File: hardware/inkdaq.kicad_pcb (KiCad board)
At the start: 2 copper layers, 13.5 x 42.5 mm, 3 parts, among them U1 INA333xxDRG

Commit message: route pcb
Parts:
- removed R1: 2.05k, Resistor_SMD:R_0201_0603Metric
- removed U1: INA333xxDRG, Package_SON:WSON-8-1EP_3x3mm_P0.5mm_EP1.45x2.4mm
- added C1: 100nF, Capacitor_SMD:C_0201_0603Metric, F.Cu at (179.1, 126.7)
- added J1: Conn_01x01, inkdaq_footprints:WirePad_1mm_Square, F.Cu at (180.8, 133.0)
- added J2: Conn_01x01, inkdaq_footprints:WirePad_1mm_Square, F.Cu at (176.4, 132.8)
- added J3: Conn_01x01, inkdaq_footprints:WirePad_1mm_Square, F.Cu at (177.9, 133.2)
- added J4: Conn_01x01, inkdaq_footprints:WirePad_1mm_Square, F.Cu at (179.3, 133.3)
- moved B1 49.1 mm to (178.8, 131.1)
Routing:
- net HSFPAR_V_NEG: track 33.7 -> 6.00 mm, vias 2 -> 0
- net HSFPAR_V_POS: track 32.1 -> 4.60 mm
- net GND: track 8.10 -> 4.18 mm
- net VDD: track 9.80 -> 6.86 mm
- net Net-(R1-Pad1): track 2.24 -> 0.00 mm
- net Net-(R1-Pad2): track 2.16 -> 0.00 mm
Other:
- board size 13.5 x 42.5 mm -> 12 x 12 mm

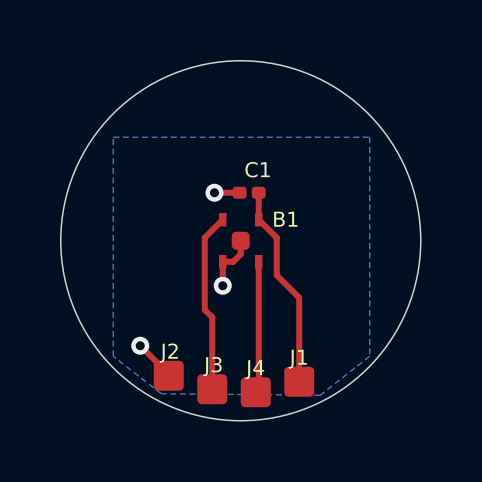
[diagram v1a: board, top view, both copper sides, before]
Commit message: make pcb 3mm radius and not 6mm (i thought it was the diameter lol)
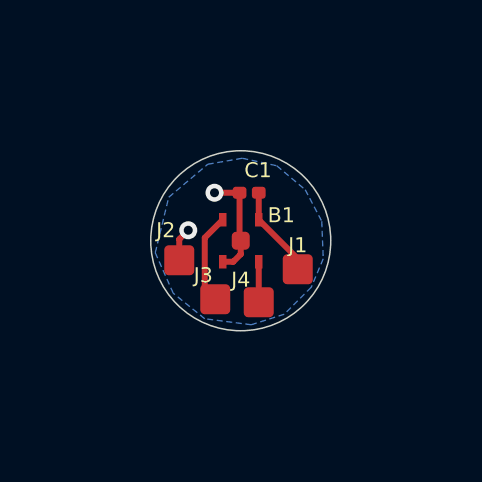
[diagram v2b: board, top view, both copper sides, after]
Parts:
- moved J2 3.87 mm to (176.8, 128.9)
- moved J1 3.75 mm to (180.8, 129.2)
- moved J3 3.00 mm to (178.0, 130.2)
- moved J4 3.00 mm to (179.4, 130.3)
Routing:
- net VDD: track 6.86 -> 3.09 mm
- net HSFPAR_V_POS: track 4.60 -> 1.35 mm
- net HSFPAR_V_NEG: track 6.00 -> 3.04 mm
- net GND: track 4.18 -> 4.73 mm, vias 3 -> 2
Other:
- board size 12 x 12 mm -> 6 x 6 mm
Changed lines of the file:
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@@
 	(footprint "inkdaq_footprints:WirePad_1mm_Square"
 		(layer "F.Cu")
-		(at 176.45 132.8)
+		(at 176.8 128.95)
 		(property "Reference" "J2"
-			(at 0.05 -0.8 0)
+			(at -0.45 -1 0)
 			(unlocked yes)
 			(layer "F.SilkS")
@@
 	(footprint "inkdaq_footprints:WirePad_1mm_Square"
 		(layer "F.Cu")
-		(at 180.8 133)
+		(at 180.75 129.25)
 		(property "Reference" "J1"
 			(at 0 -0.8 0)
@@
 	(footprint "inkdaq_footprints:WirePad_1mm_Square"
 		(layer "F.Cu")
-		(at 177.9 133.25)
+		(at 178 130.25)
 		(property "Reference" "J3"
-			(at 0.05 -0.8 0)
+			(at -0.4 -0.8 0)
 			(unlocked yes)
 			(layer "F.SilkS")
@@
 	(footprint "inkdaq_footprints:WirePad_1mm_Square"
 		(layer "F.Cu")
-		(at 179.35 133.35)
+		(at 179.45 130.35)
 		(property "Reference" "J4"
-			(at 0 -0.8 0)
+			(at -0.6 -0.75 0)
 			(unlocked yes)
 			(layer "F.SilkS")
@@
 		(descr "ALPSALPINE HSFPAR Series High-sensitivity Force Sensor")
 		(property "Reference" "B1"
-			(at 1.5 -3.45 0)
+			(at 1.35 -3.6 0)
 			(unlocked yes)
 			(layer "F.SilkS")
@@
 	(gr_circle
 		(center 178.85 128.3)
-		(end 184.85 128.3)
+		(end 181.85 128.3)
 		(stroke
 			(width 0.05)
@@
 	)
 	(segment
+		(start 178.81 128.26)
+		(end 178.85 128.3)
+		(width 0.2)
+		(layer "F.Cu")
+		(net 1)
+	)
+	(segment
 		(start 178.6 129)
 		(end 178.25 129)
@@
 	)
 	(segment
-		(start 176.45 132.8)
-		(end 176.45 132.75)
-		(width 0.2)
-		(layer "F.Cu")
-		(net 1)
-	)
-	(segment
-		(start 178.25 129.8)
-		(end 178.25 129)
-		(width 0.2)
-		(layer "F.Cu")
-		(net 1)
-	)
-	(segment
 		(start 178.85 128.75)
 		(end 178.6 129)
@@
 	)
 	(segment
+		(start 177.1 127.95)
+		(end 176.8 128.25)
+		(width 0.2)
+		(layer "F.Cu")
+		(net 1)
+	)
+	(segment
 		(start 177.975 126.7)
 		(end 178.81 126.7)
@@
 	)
 	(segment
-		(start 176.45 132.75)
-		(end 175.5 131.8)
+		(start 176.8 128.25)
+		(end 176.8 128.95)
+		(width 0.2)
+		(layer "F.Cu")
+		(net 1)
+	)
+	(segment
+		(start 178.81 126.7)
+		(end 178.81 128.26)
 		(width 0.2)
 		(layer "F.Cu")
@@
 	)
 	(via
-		(at 175.5 131.8)
+		(at 177.1 127.95)
 		(size 0.6)
 		(drill 0.3)
@@
 		(net 1)
 	)
-	(via
-		(at 178.25 129.8)
-		(size 0.6)
-		(drill 0.3)
-		(layers "F.Cu" "B.Cu")
-		(free yes)
-		(net 1)
-	)
-	(segment
-		(start 179.45 133.4)
-		(end 179.3 133.55)
+	(segment
+		(start 179.45 129)
+		(end 179.45 130.35)
 		(width 0.2)
 		(layer "F.Cu")
@@
 	)
 	(segment
-		(start 179.45 129)
-		(end 179.45 133.25)
-		(width 0.2)
-		(layer "F.Cu")
-		(net 2)
-	)
-	(segment
-		(start 179.45 133.25)
-		(end 179.35 133.35)
-		(width 0.2)
-		(layer "F.Cu")
-		(net 2)
-	)
-	(segment
-		(start 179.45 127.6)
-		(end 180.05 128.2)
-		(width 0.2)
-		(layer "F.Cu")
-		(net 3)
-	)
-	(segment
-		(start 180.05 128.2)
-		(end 180.05 129.45)
+		(start 180.75 128.9)
+		(end 180.75 129.25)
 		(width 0.2)
 		(layer "F.Cu")
@@
 	)
 	(segment
-		(start 180.8 130.2)
-		(end 180.8 133)
+		(start 179.45 127.6)
+		(end 180.75 128.9)
 		(width 0.2)
 		(layer "F.Cu")
@@
 	)
 	(segment
-		(start 180.05 129.45)
-		(end 180.8 130.2)
-		(width 0.2)
-		(layer "F.Cu")
-		(net 3)
-	)
-	(segment
-		(start 177.65 128.2)
-		(end 177.65 130.6)
-		(width 0.2)
-		(layer "F.Cu")
-		(net 4)
-	)
-	(segment
-		(start 177.65 130.6)
-		(end 177.9 130.85)
+		(start 177.65 129.9)
+		(end 178 130.25)
 		(width 0.2)
 		(layer "F.Cu")
@@
 	)
 	(segment
-		(start 177.9 130.85)
-		(end 177.9 133.25)
+		(start 177.65 128.2)
+		(end 177.65 129.9)
 		(width 0.2)
 		(layer "F.Cu")
@@
 		(polygon
 			(pts
-				(xy 183.15 124.85) (xy 183.15 132.15) (xy 181.5 133.45) (xy 176.2 133.4) (xy 174.6 132.15) (xy 174.6 124.85)
-			)
-		)
+				(xy 176 128.7) (xy 176.45 126.85) (xy 177.75 125.75) (xy 178.9 125.55) (xy 180.05 125.8) (xy 181 126.6)
+				(xy 181.55 127.65) (xy 181.6 128.9) (xy 181.2 129.85) (xy 180.3 130.75) (xy 179.2 131.1) (xy 177.65 130.9)
+				(xy 176.6 130.05)
+			)
+		)

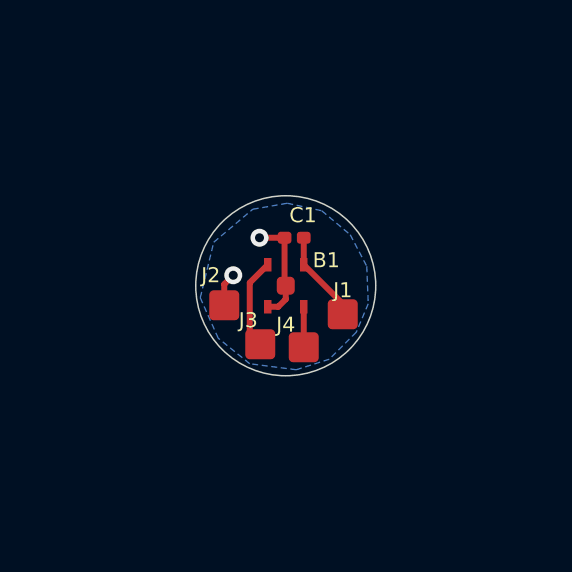
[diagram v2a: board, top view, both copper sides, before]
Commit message: pcb: panelize in order to be able to use JLCPCBA
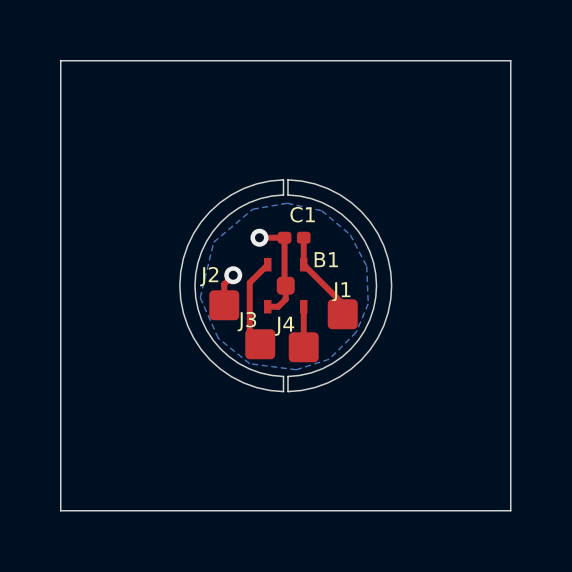
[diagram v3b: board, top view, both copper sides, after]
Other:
- board size 6 x 6 mm -> 15 x 15 mm
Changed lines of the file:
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@@
 	(title_block
 		(title "InkDAQ - Pen sensor board")
-		(date "2026-03-02")
-		(rev "2.0")
+		(date "2026-03-07")
+		(rev "2.1")
 		(company "Stratos Thivaios")
 		(comment 1 "CERN Open Hardware License v2 - Strongly Reciprocal")
@@
 		)
 	)
-	(gr_circle
-		(center 178.85 128.3)
-		(end 181.85 128.3)
+	(gr_arc
+		(start 178.774908 131.829339)
+		(mid 175.319862 128.299954)
+		(end 178.775 124.770659)
+		(stroke
+			(width 0.05)
+			(type default)
+		)
+		(layer "Edge.Cuts")
+	)
+	(gr_arc
+		(start 178.925 124.770659)
+		(mid 182.380138 128.299954)
+		(end 178.925092 131.829339)
+		(stroke
+			(width 0.05)
+			(type default)
+		)
+		(layer "Edge.Cuts")
+	)
+	(gr_arc
+		(start 178.775 131.324999)
+		(mid 175.824071 128.3)
+		(end 178.775 125.275001)
+		(stroke
+			(width 0.05)
+			(type default)
+		)
+		(layer "Edge.Cuts")
+	)
+	(gr_line
+		(start 178.925 124.770659)
+		(end 178.925 125.275)
+		(stroke
+			(width 0.05)
+			(type default)
+		)
+		(layer "Edge.Cuts")
+	)
+	(gr_line
+		(start 178.775 124.770659)
+		(end 178.775 125.275)
+		(stroke
+			(width 0.05)
+			(type default)
+		)
+		(layer "Edge.Cuts")
+	)
+	(gr_line
+		(start 178.925648 131.324983)
+		(end 178.925 131.825)
+		(stroke
+			(width 0.05)
+			(type default)
+		)
+		(layer "Edge.Cuts")
+	)
+	(gr_line
+		(start 178.775 131.324999)
+		(end 178.775 131.825)
+		(stroke
+			(width 0.05)
+			(type default)
+		)
+		(layer "Edge.Cuts")
+	)
+	(gr_rect
+		(start 171.35 120.8)
+		(end 186.35 135.8)
 		(stroke
 			(width 0.05)
@@
 		(layer "Edge.Cuts")
 	)
+	(gr_arc
+		(start 178.925 125.275)
+		(mid 181.87593 128.299676)
+		(end 178.925648 131.324984)
+		(stroke
+			(width 0.05)
+			(type default)
+		)
+		(layer "Edge.Cuts")
+	)

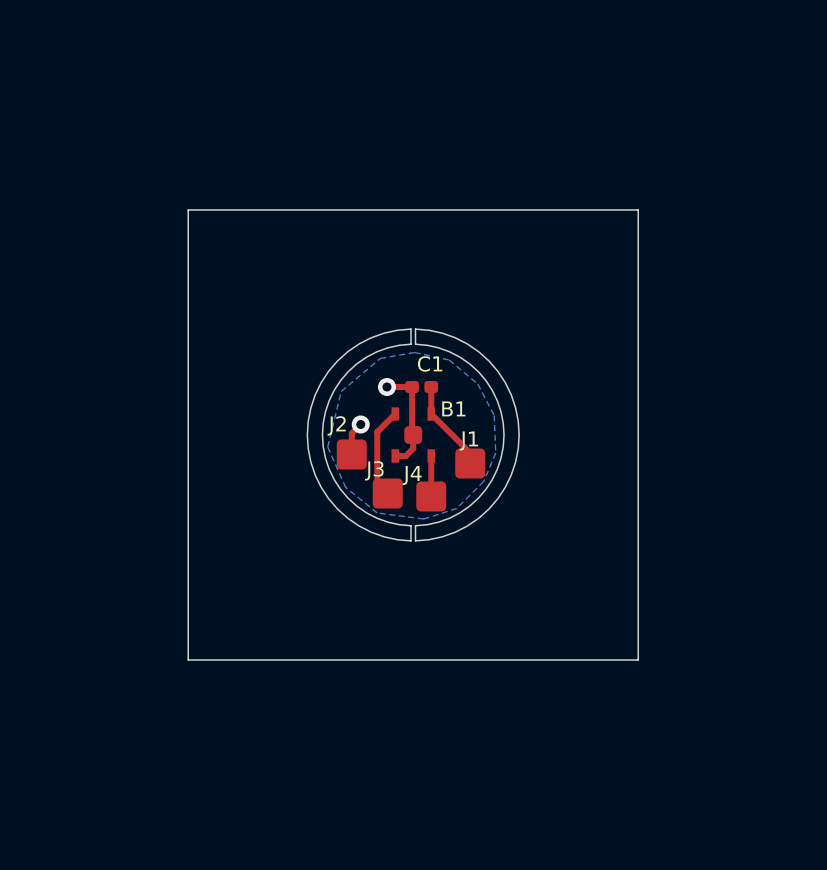
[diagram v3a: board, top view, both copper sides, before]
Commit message: pcb: larger panel, generate v2.2 gerbers
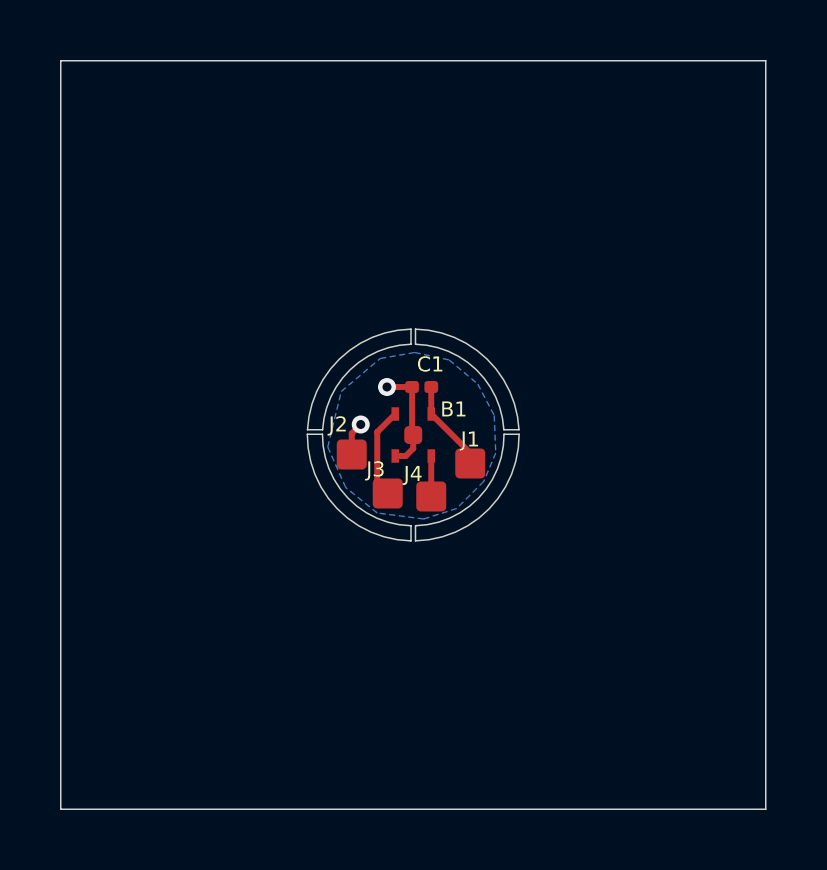
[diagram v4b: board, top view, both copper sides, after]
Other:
- board size 15 x 15 mm -> 23.5 x 25 mm
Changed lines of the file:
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@@
 		(title "InkDAQ - Pen sensor board")
 		(date "2026-03-07")
-		(rev "2.1")
+		(rev "2.2")
 		(company "Stratos Thivaios")
 		(comment 1 "CERN Open Hardware License v2 - Strongly Reciprocal")
@@
 		)
 	)
+	(gr_line
+		(start 175.325 128.125)
+		(end 175.829118 128.125306)
+		(stroke
+			(width 0.05)
+			(type default)
+		)
+		(layer "Edge.Cuts")
+	)
 	(gr_arc
-		(start 178.774908 131.829339)
-		(mid 175.319862 128.299954)
-		(end 178.775 124.770659)
+		(start 175.829118 128.125292)
+		(mid 176.745918 126.125353)
+		(end 178.775 125.275)
 		(stroke
 			(width 0.05)
@@
 	)
 	(gr_arc
-		(start 178.925 124.770659)
-		(mid 182.380138 128.299954)
-		(end 178.925092 131.829339)
+		(start 178.774997 131.325102)
+		(mid 176.675207 130.404078)
+		(end 175.824071 128.275)
 		(stroke
 			(width 0.05)
@@
 	)
 	(gr_arc
-		(start 178.775 131.324999)
-		(mid 175.824071 128.3)
-		(end 178.775 125.275001)
+		(start 175.325 128.125)
+		(mid 176.390013 125.769246)
+		(end 178.775017 124.771456)
+		(stroke
+			(width 0.05)
+			(type default)
+		)
+		(layer "Edge.Cuts")
+	)
+	(gr_arc
+		(start 178.774903 131.82956)
+		(mid 176.31852 130.760699)
+		(end 175.31973 128.275)
 		(stroke
 			(width 0.05)
@@
 	)
 	(gr_line
-		(start 178.925 124.770659)
+		(start 178.924953 124.771456)
 		(end 178.925 125.275)
 		(stroke
@@
 	)
 	(gr_line
-		(start 178.775 124.770659)
+		(start 178.775 124.771456)
 		(end 178.775 125.275)
+		(stroke
+			(width 0.05)
+			(type default)
+		)
+		(layer "Edge.Cuts")
+	)
+	(gr_line
+		(start 181.875 128.275)
+		(end 182.379341 128.275)
 		(stroke
 			(width 0.05)
@@
 	(gr_line
 		(start 178.925648 131.324983)
-		(end 178.925 131.825)
+		(end 178.925077 131.828631)
+		(stroke
+			(width 0.05)
+			(type default)
+		)
+		(layer "Edge.Cuts")
+	)
+	(gr_arc
+		(start 178.924983 124.771456)
+		(mid 181.309986 125.769247)
+		(end 182.375 128.125)
 		(stroke
 			(width 0.05)
@@
 	(gr_line
 		(start 178.775 131.324999)
-		(end 178.775 131.825)
+		(end 178.775 131.829561)
+		(stroke
+			(width 0.05)
+			(type default)
+		)
+		(layer "Edge.Cuts")
+	)
+	(gr_arc
+		(start 181.875928 128.275)
+		(mid 181.025018 130.403845)
+		(end 178.925651 131.325085)
+		(stroke
+			(width 0.05)
+			(type default)
+		)
+		(layer "Edge.Cuts")
+	)
+	(gr_line
+		(start 181.870659 128.125)
+		(end 182.375 128.125)
 		(stroke
 			(width 0.05)
@@
 	)
 	(gr_rect
-		(start 171.35 120.8)
-		(end 186.35 135.8)
+		(start 167.1 115.825)
+		(end 190.6 140.775)
 		(stroke
 			(width 0.05)
@@
 	)
 	(gr_arc
-		(start 178.925 125.275)
-		(mid 181.87593 128.299676)
-		(end 178.925648 131.324984)
-		(stroke
-			(width 0.05)
+		(start 182.379341 128.275)
+		(mid 181.380816 130.760049)
+		(end 178.925077 131.828631)
+		(stroke
+			(width 0.05)
+			(type default)
+		)
+		(layer "Edge.Cuts")
+	)
+	(gr_line
+		(start 175.31973 128.275)
+		(end 175.824071 128.275)
+		(stroke
+			(width 0.05)
+			(type default)
+		)
+		(layer "Edge.Cuts")
+	)
+	(gr_arc
+		(start 178.924995 125.275206)
+		(mid 180.95383 126.125396)
+		(end 181.870659 128.125)
+		(stroke
+			(width 0.05)
